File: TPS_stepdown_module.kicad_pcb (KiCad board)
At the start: 2 copper layers, 58.4 x 21.6 mm, 32 parts, among them J1 Vin, J2 Gnd, J3 Gnd, J4 Vout, U1 TPS54360DDA

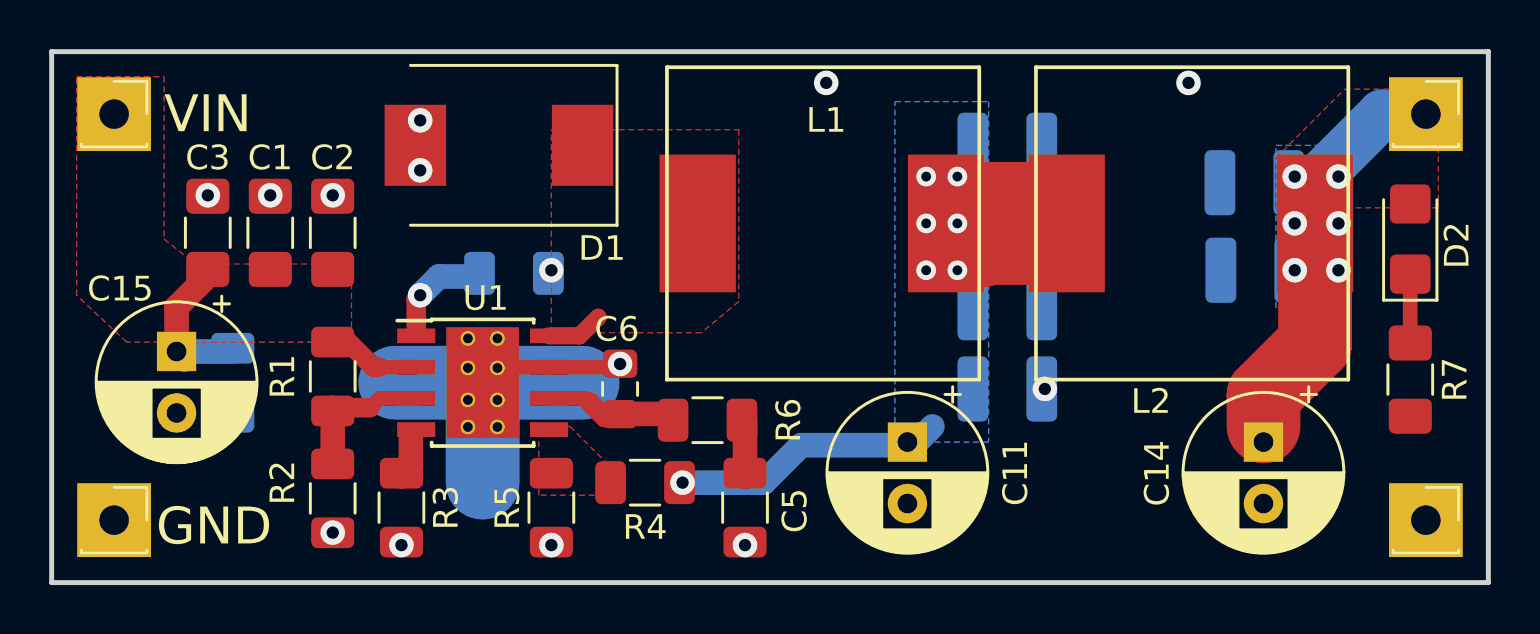
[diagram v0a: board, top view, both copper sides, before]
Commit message: изменил размеры входной керамики
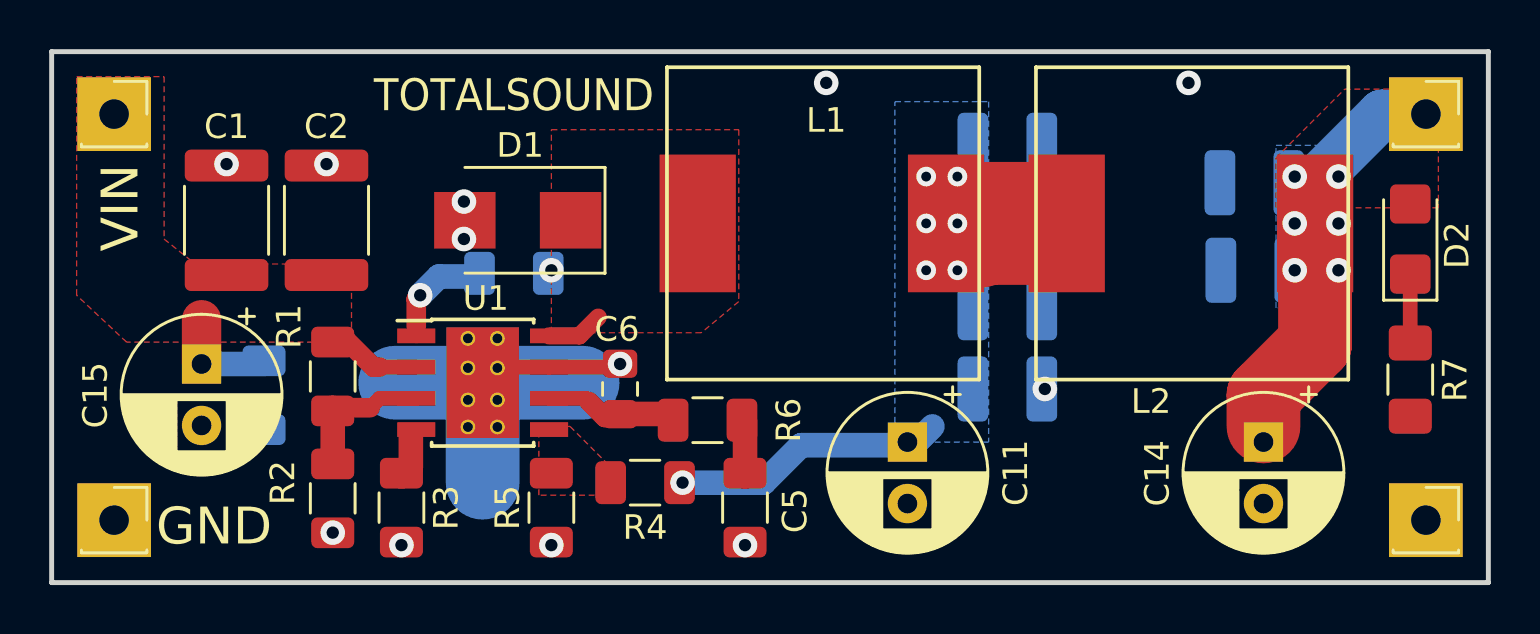
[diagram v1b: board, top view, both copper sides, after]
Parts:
- removed C3: 2.2uF_100V, Capacitor_SMD:C_1206_3216Metric_Pad1.42x1.75mm_HandSolder
- C1, C2: footprint Capacitor_SMD:C_1206_3216Metric_Pad1.42x1.75mm_HandSolder -> Capacitor_SMD:C_1812_4532Metric_Pad1.30x3.40mm_HandSolder
- D1: value STPS5L60S -> SK56; footprint Diode_SMD:D_SMC -> Diode_SMD:D_SMB
- L1: value 10uH -> 15uH
- R1: value 500K -> 510K
- R2: value 100K -> 82K
- moved D1 3.14 mm to (60.9, 78.0)
- moved C1 1.85 mm to (49.0, 78.0)
- moved C16 1.37 mm to (50.5, 85.1)
- moved C15 1.14 mm to (48.0, 83.8)
- moved C2 0.57 mm to (53.1, 78.0)
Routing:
- net Net-(C1-Pad1): track 10.5 -> 8.21 mm
- net GND: vias 13 -> 12
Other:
- board text added: "TOTALSOUND"
